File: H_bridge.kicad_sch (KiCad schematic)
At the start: 39 parts

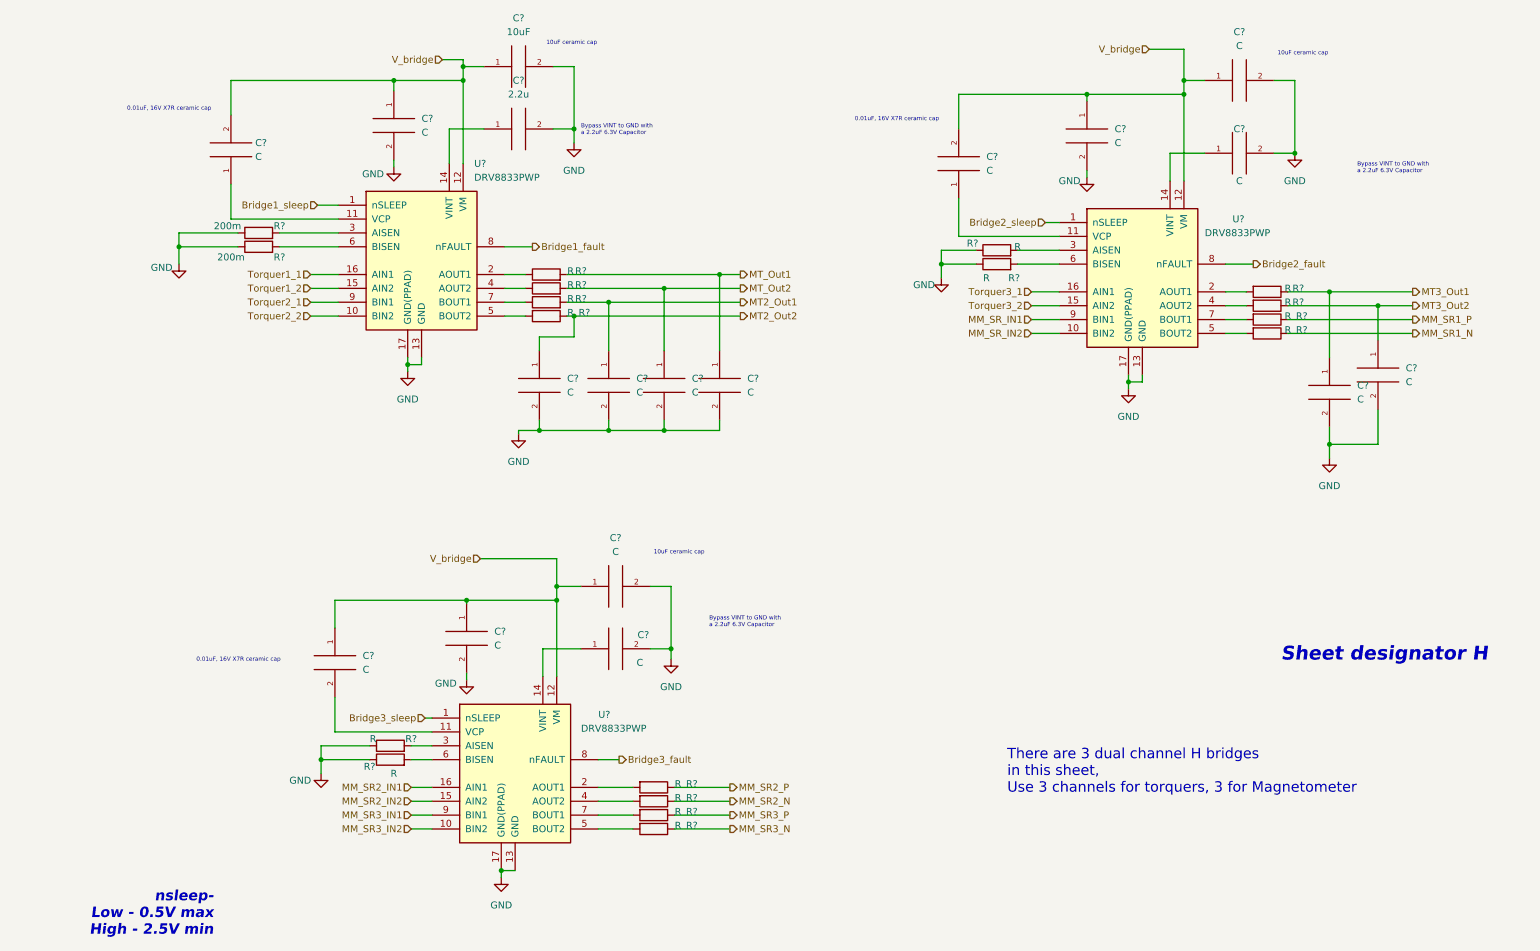
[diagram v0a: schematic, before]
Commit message: added hbridge designators and sense res values
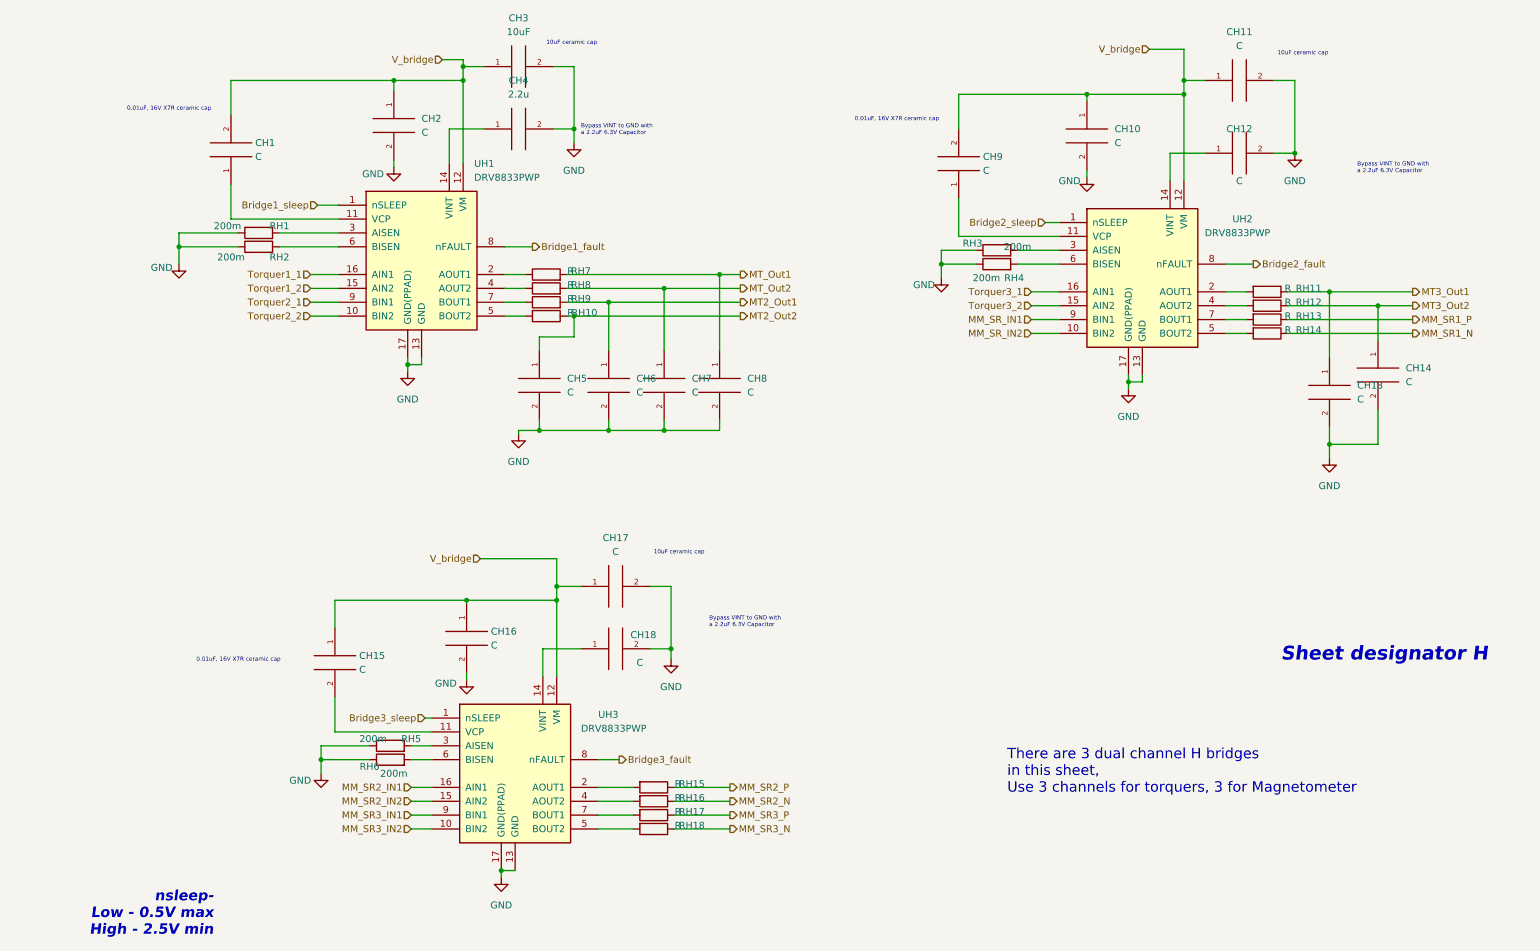
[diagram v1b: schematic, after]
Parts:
- RH3, RH4, RH5, RH6: renamed from R?; value R -> 200m
- gave numbers to parts that had none: 35

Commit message: add power and processor and connectors
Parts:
- CH1, CH15, CH9: value C -> 0.01u
- CH11, CH17: value C -> 10u
- CH12, CH18: value C -> 2.2u
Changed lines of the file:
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@@
     (in_bom yes) (on_board yes) (fields_autoplaced)
     (property "Reference" "CH11" (id 0) (at 227.33 24.13 90))
-    (property "Value" "C" (id 1) (at 227.33 26.67 90))
+    (property "Value" "10u" (id 1) (at 227.33 26.67 90))
     (property "Footprint" "" (id 2) (at 227.33 33.02 0)
       (effects (font (size 1.27 1.27)) hide)
@@
       (effects (font (size 1.27 1.27)) (justify left))
     )
-    (property "Value" "C" (id 1) (at 66.04 140.9699 0)
+    (property "Value" "0.01u" (id 1) (at 66.04 140.9699 0)
       (effects (font (size 1.27 1.27)) (justify left))
     )
@@
       (effects (font (size 1.27 1.27)) (justify right))
     )
-    (property "Value" "C" (id 1) (at 180.34 49.5299 0)
+    (property "Value" "0.01u" (id 1) (at 180.34 49.5299 0)
       (effects (font (size 1.27 1.27)) (justify right))
     )
@@
     (in_bom yes) (on_board yes) (fields_autoplaced)
     (property "Reference" "CH17" (id 0) (at 113.03 116.84 90))
-    (property "Value" "C" (id 1) (at 113.03 119.38 90))
+    (property "Value" "10u" (id 1) (at 113.03 119.38 90))
     (property "Footprint" "" (id 2) (at 113.03 125.73 0)
       (effects (font (size 1.27 1.27)) hide)
@@
     (in_bom yes) (on_board yes)
     (property "Reference" "CH18" (id 0) (at 118.11 134.62 90))
-    (property "Value" "C" (id 1) (at 117.475 139.7 90))
+    (property "Value" "2.2u" (id 1) (at 117.475 139.7 90))
     (property "Footprint" "" (id 2) (at 113.03 137.16 0)
       (effects (font (size 1.27 1.27)) hide)
@@
     (in_bom yes) (on_board yes)
     (property "Reference" "CH12" (id 0) (at 227.33 41.91 90))
-    (property "Value" "C" (id 1) (at 227.33 51.435 90))
+    (property "Value" "2.2u" (id 1) (at 227.33 51.435 90))
     (property "Footprint" "" (id 2) (at 227.33 46.355 0)
       (effects (font (size 1.27 1.27)) hide)
@@
       (effects (font (size 1.27 1.27)) (justify right))
     )
-    (property "Value" "C" (id 1) (at 46.99 46.9899 0)
+    (property "Value" "0.01u" (id 1) (at 46.99 46.9899 0)
       (effects (font (size 1.27 1.27)) (justify right))
     )

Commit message: MCU interfaces are done! Check the Changes and Complete ERC modifications
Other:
- company: (none) -> Parikshit Student Satellite Team
- title: (none) -> AOCS BOARD
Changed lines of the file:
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@@
 (kicad_sch (version 20211123) (generator eeschema)
   (paper "A4")
+  (title_block
+    (title "AOCS BOARD")
+    (company "Parikshit Student Satellite Team")
+  )
   (junction (at 111.76 73.66) (diameter 0) (color 0 0 0 0)
   )
@@
   )
   (wire (pts (xy 105.41 76.2) (xy 135.89 76.2))
+    (stroke (width 0) (type default) (color 0 0 0 0))
+  )
+  (wire (pts (xy 20.955 125.095) (xy 20.955 123.825))
     (stroke (width 0) (type default) (color 0 0 0 0))
   )
@@
     (pin "1")
     (pin "2")
+  )
+  (symbol (lib_id "power:GND") (at 20.955 125.095 0) (unit 1)
+    (in_bom yes) (on_board yes) (fields_autoplaced)
+    (property "Reference" "#PWR0270" (id 0) (at 20.955 131.445 0)
+      (effects (font (size 1.27 1.27)) hide)
+    )
+    (property "Value" "GND" (id 1) (at 20.955 129.54 0))
+    (property "Footprint" "" (id 2) (at 20.955 125.095 0)
+      (effects (font (size 1.27 1.27)) hide)
+    )
+    (property "Datasheet" "" (id 3) (at 20.955 125.095 0)
+      (effects (font (size 1.27 1.27)) hide)
+    )
+    (pin "1")
   )
   (symbol (lib_id "pspice:C") (at 227.33 33.02 90) (unit 1)
@@
     (pin "2")
   )
+  (symbol (lib_id "power:PWR_FLAG") (at 20.955 123.825 0) (unit 1)
+    (in_bom yes) (on_board yes) (fields_autoplaced)
+    (property "Reference" "#FLG0106" (id 0) (at 20.955 121.92 0)
+      (effects (font (size 1.27 1.27)) hide)
+    )
+    (property "Value" "PWR_FLAG" (id 1) (at 20.955 118.11 0))
+    (property "Footprint" "" (id 2) (at 20.955 123.825 0)
+      (effects (font (size 1.27 1.27)) hide)
+    )
+    (property "Datasheet" "~" (id 3) (at 20.955 123.825 0)
+      (effects (font (size 1.27 1.27)) hide)
+    )
+    (pin "1")
+  )
   (symbol (lib_id "Device:R") (at 120.015 165.1 270) (unit 1)

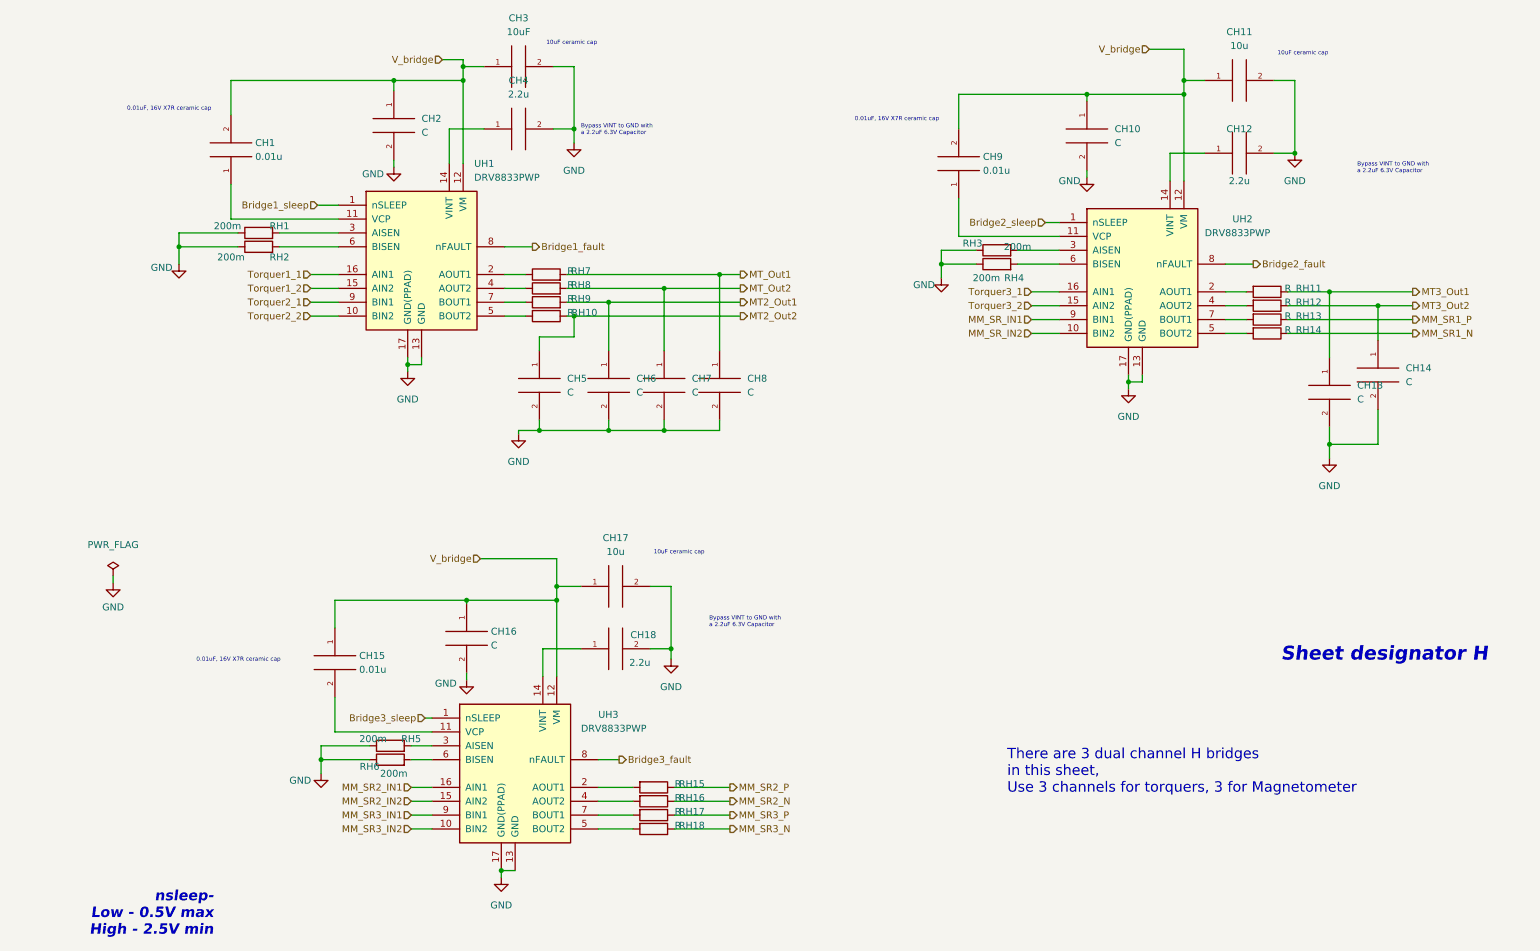
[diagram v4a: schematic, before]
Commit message: Max ERC errors corrected
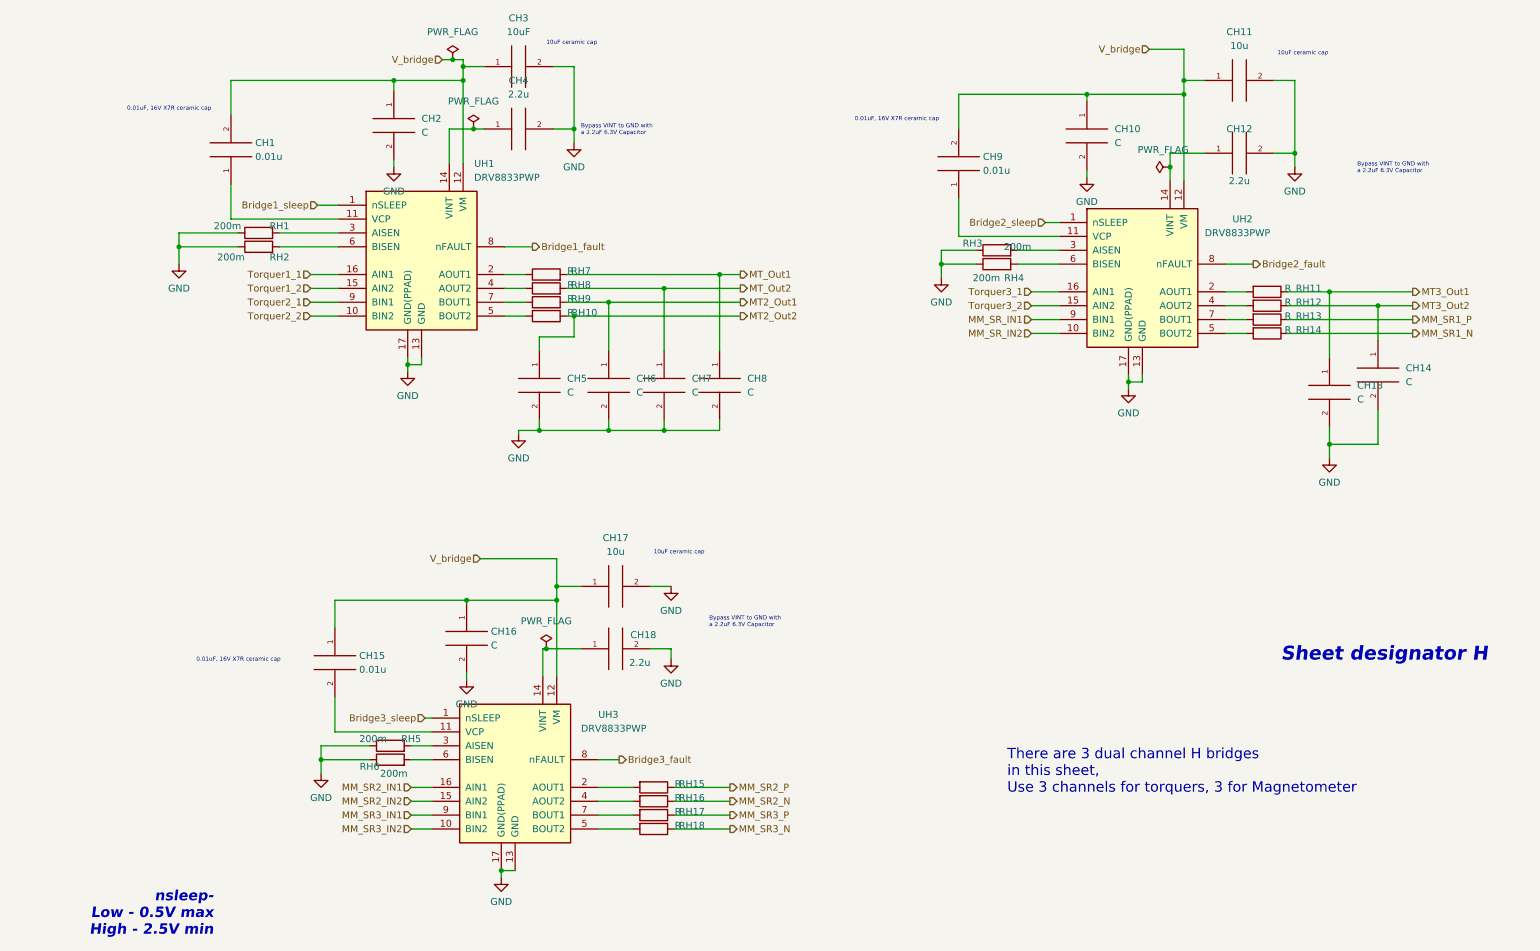
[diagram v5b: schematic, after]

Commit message: Updated the changes
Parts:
- renumbered CH3 to CH1, CH5 to CH10, CH6 to CH11, CH7 to CH12, CH8 to CH13, CH13 to CH14, CH17 to CH15, CH18 to CH17, CH15 to CH18, CH11 to CH2, CH2 to CH3, CH10 to CH5, CH1 to CH6, CH12 to CH7, CH9 to CH8, CH14 to CH9, RH13 to RH11, RH14 to RH12, RH5 to RH13, RH6 to RH14, RH7 to RH5, RH8 to RH6, RH11 to RH7, RH9 to RH8, RH12 to RH9

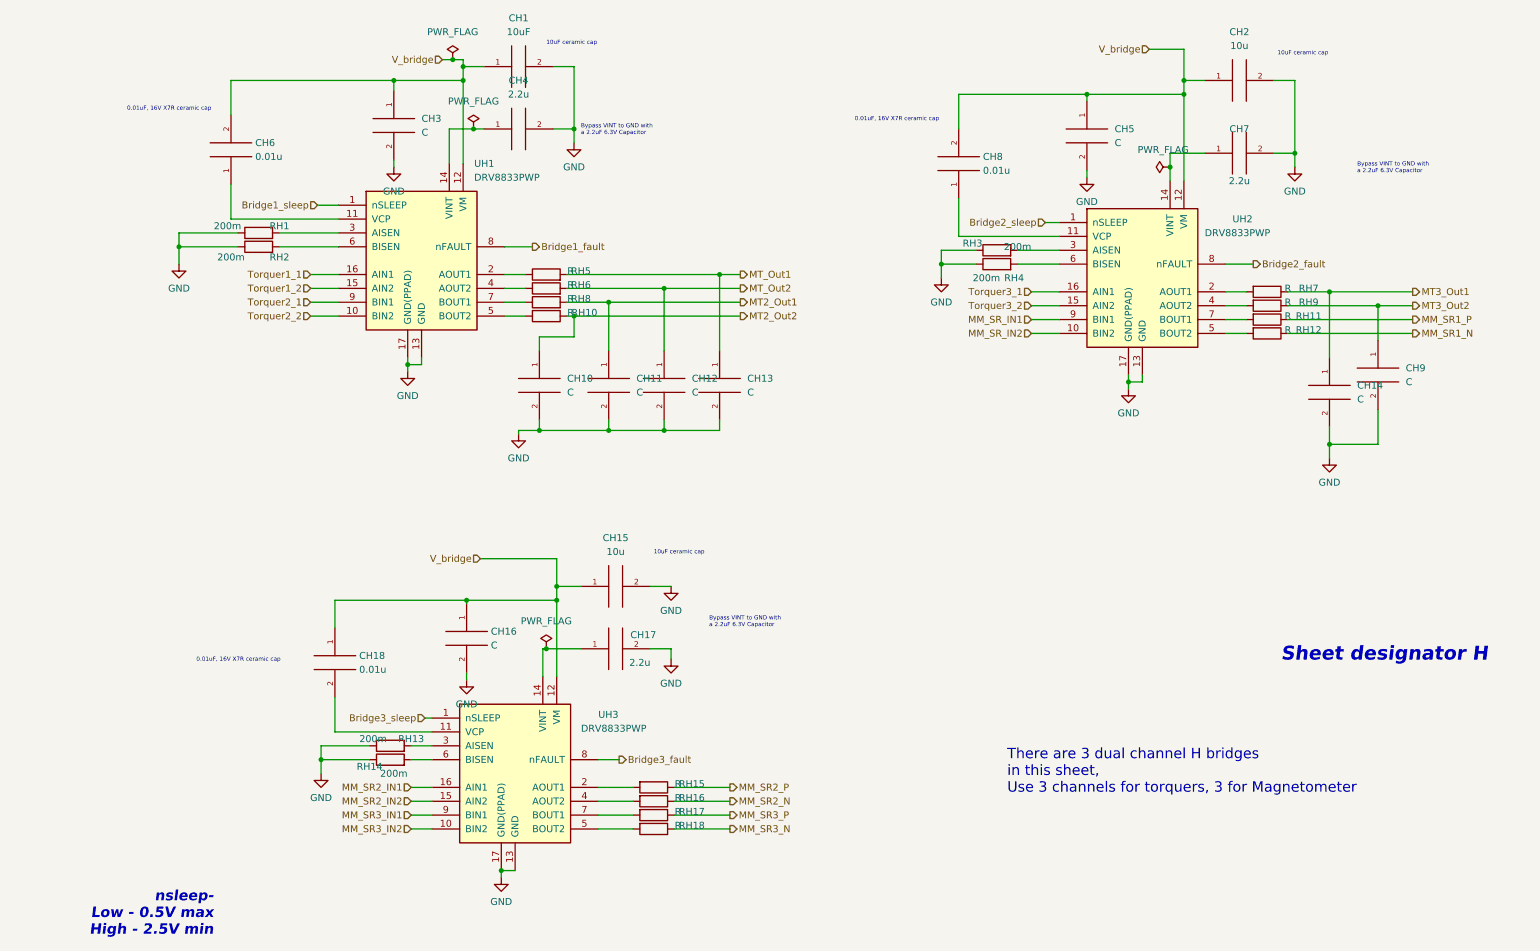
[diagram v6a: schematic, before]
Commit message: Page settings changed. Added some testpoints. Some comments are made.
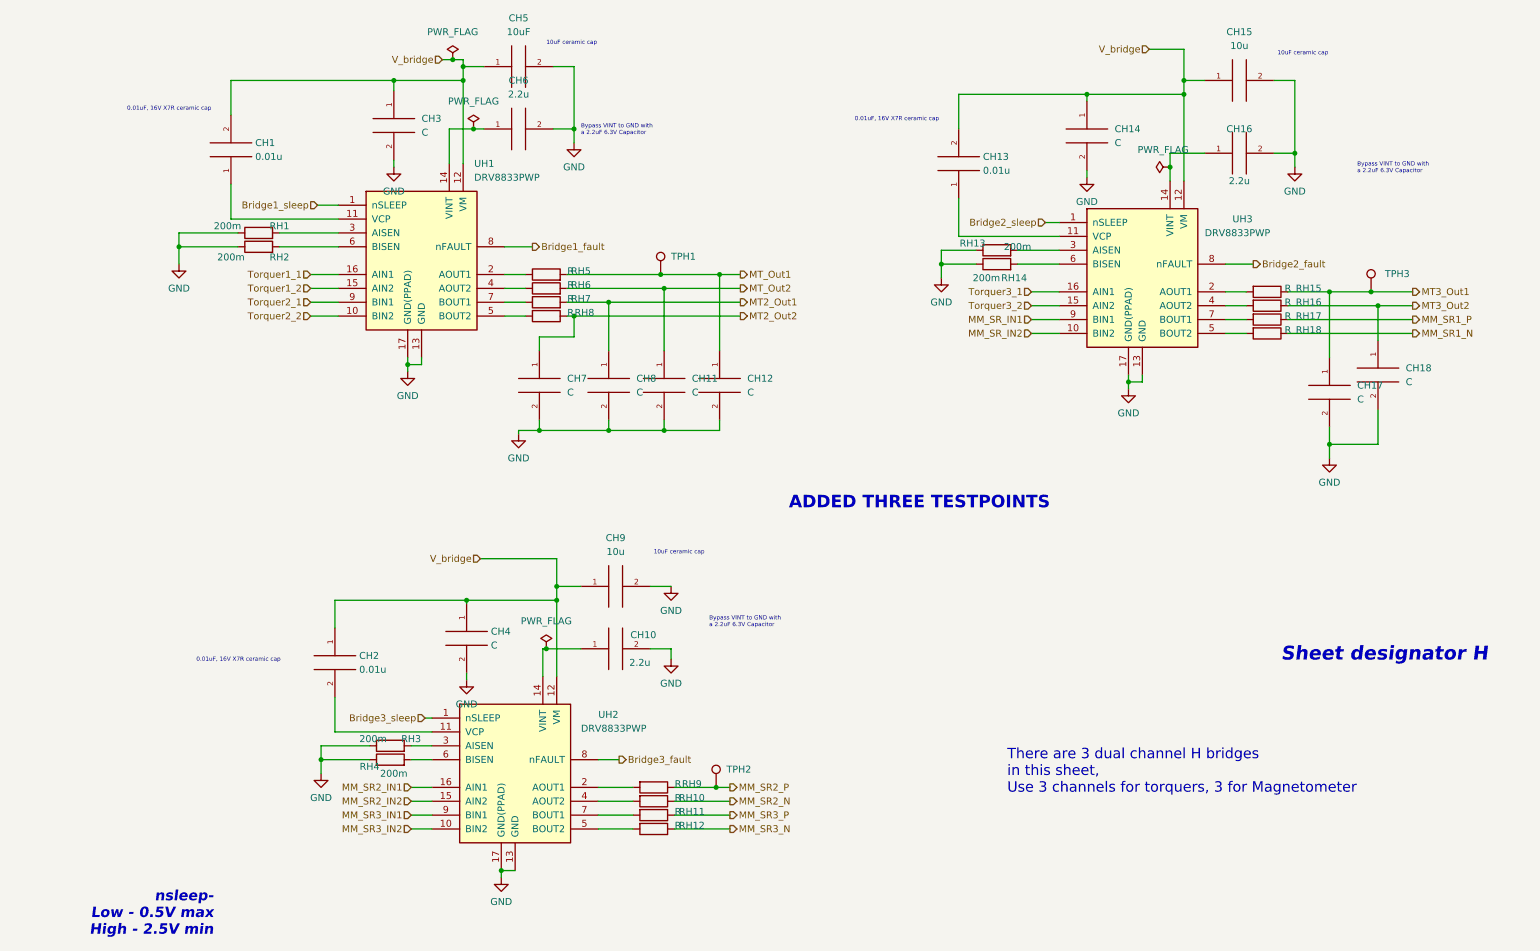
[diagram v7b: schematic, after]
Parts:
- added TPH1, TPH2, TPH3: TestPoint, TestPoint:TestPoint_Plated_Hole_D2.0mm, symbol Connector:TestPoint
- renumbered CH6 to CH1, CH17 to CH10, CH12 to CH11, CH13 to CH12, CH8 to CH13, CH5 to CH14, CH2 to CH15, CH7 to CH16, CH14 to CH17, CH9 to CH18, CH18 to CH2, CH16 to CH4, CH1 to CH5, CH4 to CH6, CH10 to CH7, CH11 to CH8, CH15 to CH9, RH16 to RH10, RH17 to RH11, RH18 to RH12, RH3 to RH13, RH4 to RH14, RH7 to RH15, RH9 to RH16, RH11 to RH17, RH12 to RH18, RH13 to RH3, RH14 to RH4, RH8 to RH7, RH10 to RH8, RH15 to RH9, UH3 to UH2, UH2 to UH3
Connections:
- net MM_SR2_P: now also TPH2.1
- net MT3_Out1: now also TPH3.1
- net MT_Out1: now also TPH1.1
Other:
- note added: "ADDED THREE TESTPOINTS"

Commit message: I2C lines are pulled up
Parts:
- CH1, CH10, CH11, CH12, CH13, CH14, CH15, CH16, CH17, CH18, CH2, CH3, CH4, CH5, CH6, CH7, CH8, CH9: footprint (none) -> Capacitor_SMD:C_0603_1608Metric
- RH1, RH10, RH11, RH12, RH13, RH14, RH15, RH16, RH17, RH18, RH2, RH3, RH4, RH5, RH6, RH7, RH8, RH9: footprint (none) -> Resistor_SMD:R_0603_1608Metric
